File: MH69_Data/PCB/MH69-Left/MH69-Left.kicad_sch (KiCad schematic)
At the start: 85 parts, among them U1 nice_nano

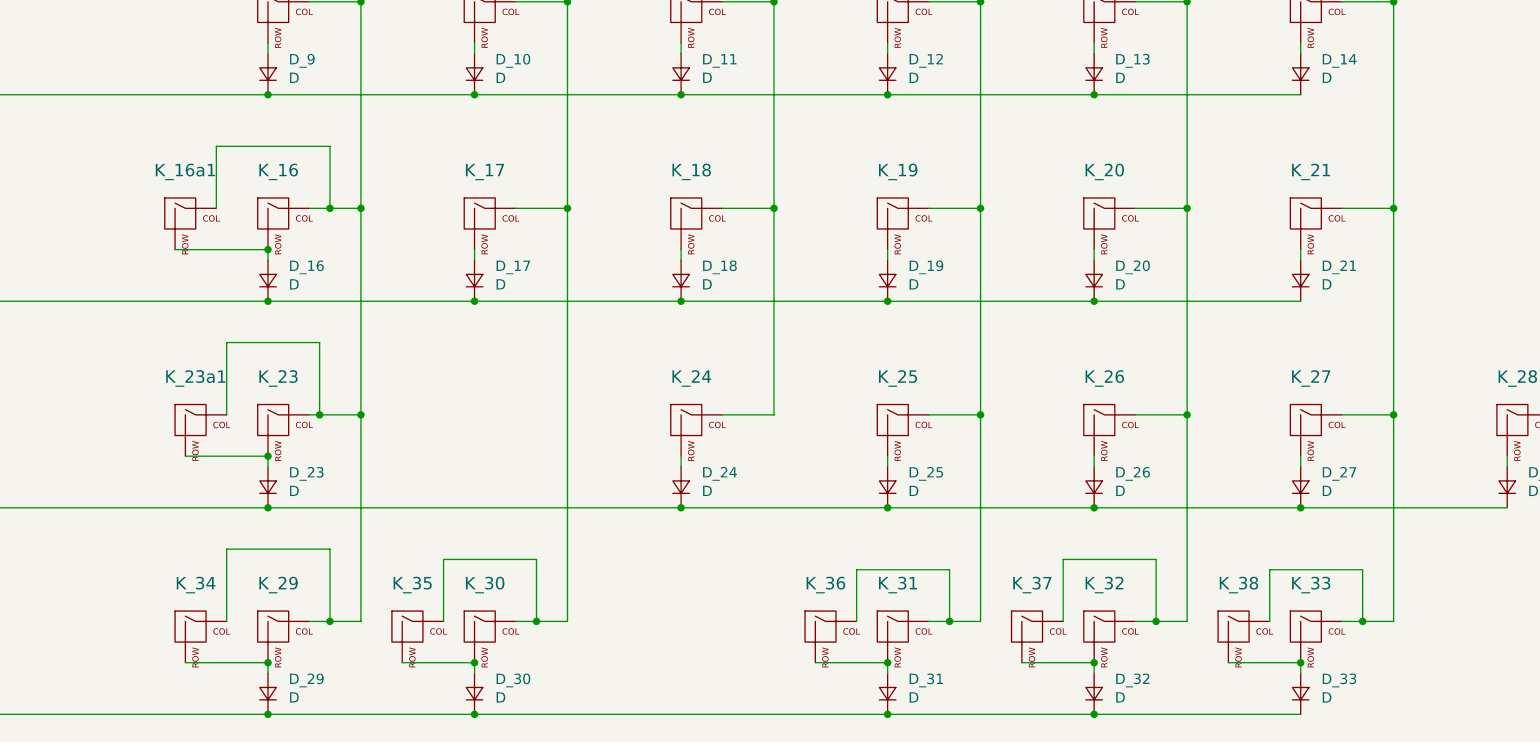
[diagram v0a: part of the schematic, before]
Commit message: Added Kailh Plated 1Us to Left
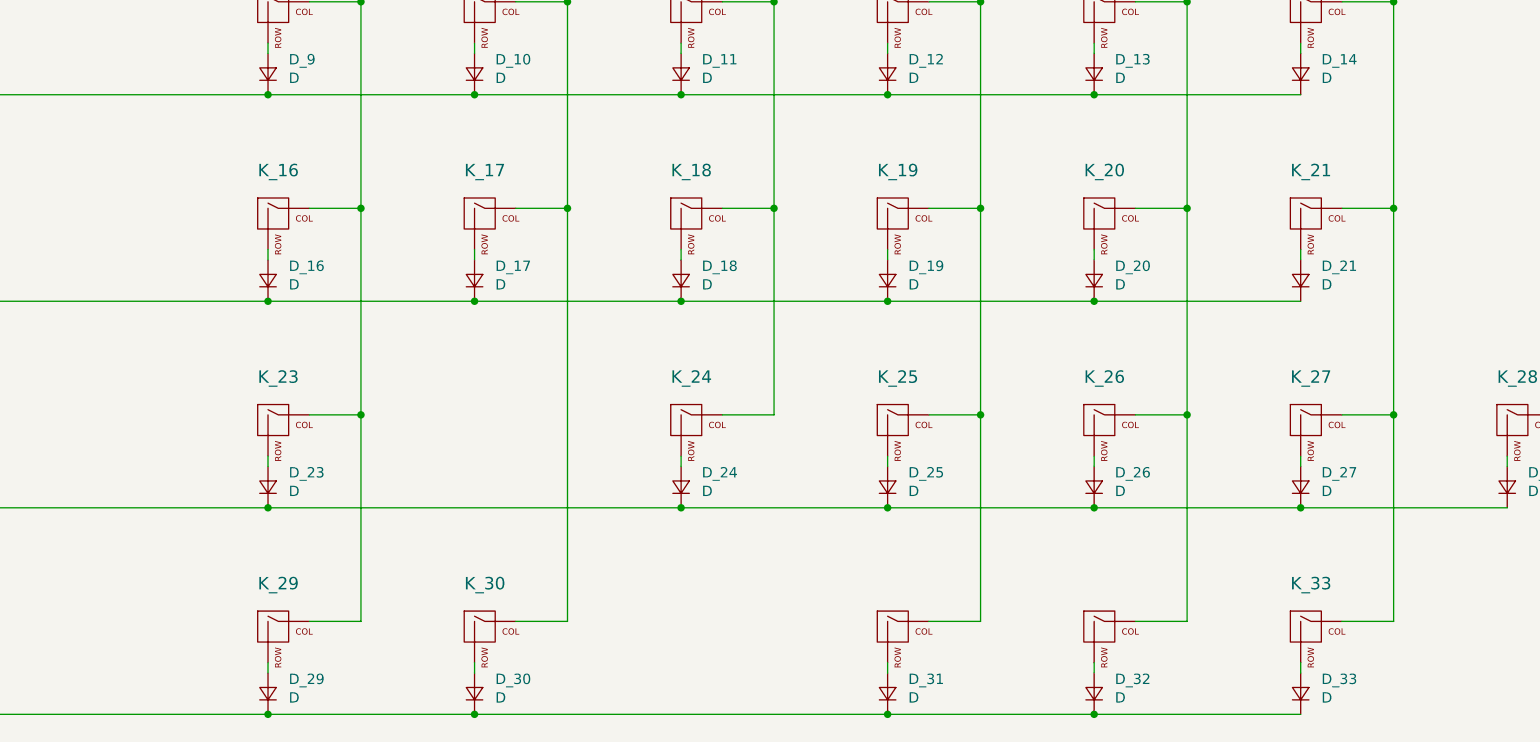
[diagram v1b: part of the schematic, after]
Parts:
- removed K_16a1: KEYSW, cb:Choc-MX-19mm-1.75u, symbol MX_Alps_Hybrid:MX-NoLED
- removed K_23a1: KEYSW, cb:Choc-MX-19mm-2.25u, symbol MX_Alps_Hybrid:MX-NoLED
- removed K_34, K_35, K_36, K_37, K_38: KEYSW, cb:Choc-MX-19mm-1.25u, symbol MX_Alps_Hybrid:MX-NoLED

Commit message: THE BIG CHANGE - schematic and PCB layout
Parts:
- added J1: OLED/E-Ink_L, Connector_PinHeader_2.54mm:PinHeader_1x05_P2.54mm_Vertical, symbol Connector_Generic:Conn_01x05
- Batt_L1: renamed from Batt1; footprint Connector_JST:JST_PH_B2B-PH-K_1x02_P2.00mm_Vertical -> Connector_PinHeader_2.54mm:PinHeader_1x02_P2.54mm_Vertical; symbol Connector:Conn_01x02_Socket -> Connector_Generic:Conn_01x02
- D_0, D_1, D_10, D_11, D_12, D_13, D_14, D_15, D_16, D_17, D_18, D_19, D_2, D_20, D_21, D_22, D_23, D_24, D_25, D_26, D_27, D_28, D_29, D_3, D_30, D_31, D_32, D_33, D_4, D_5, D_6, D_7, D_8, D_9: footprint ScottoKeebs_Components:Diode_DO-35 -> Diode_SMD:D_SOD-123
- H1, H2, H3, H4, H5, H6: footprint MountingHole:MountingHole_3.2mm_M3 -> ScottoKeebs_Scotto:Standoff_M2x6mm
- K_0, K_1, K_10, K_11, K_12, K_13, K_14, K_15, K_17, K_18, K_19, K_2, K_20, K_21, K_22, K_24, K_25, K_26, K_27, K_28, K_3, K_31, K_33, K_4, K_5, K_6, K_7, K_8: footprint cb:Choc-MX-19mm-1u -> PCM_Switch_Keyboard_Hotswap_Kailh:SW_Hotswap_Kailh_Choc_V1_Plated_1.00u
- K_16, K_23, K_30, K_32, K_9: footprint cb:Choc-MX-19mm-1.5u -> PCM_Switch_Keyboard_Hotswap_Kailh:SW_Hotswap_Kailh_Choc_V1_Plated_1.50u
- K_29: footprint cb:Choc-MX-19mm-1u -> PCM_Switch_Keyboard_Hotswap_Kailh:SW_Hotswap_Kailh_Choc_V1_Plated_1.25u
- PWR1: value POWER -> DIP_L; footprint Connector_JST:JST_PH_B2B-PH-K_1x02_P2.00mm_Vertical -> Button_Switch_SMD:SW_SPDT_PCM12; symbol Switch:SW_SPST -> Switch:SW_SPDT
- RST1: footprint Connector_JST:JST_PH_B2B-PH-K_1x02_P2.00mm_Vertical -> Button_Switch_SMD:SW_SPST_TL3342; symbol Switch:SW_SPST -> Switch:SW_Push
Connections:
- net CS_L: now reaches U1.1 (TX0/P0.06)
- net CS_L: now also J1.5 (Pin_5)
- net col2_L: now reaches U1.18 (AIN0/P0.02)
- net col2_L: now also K_10.1 (COL), K_17.1 (COL), K_2.1 (COL), K_30.1 (COL)
- net col1_L: now reaches U1.19 (AIN5/P0.29)
- net col1_L: now also K_1.1 (COL), K_16.1 (COL), K_23.1 (COL), K_29.1 (COL), K_9.1 (COL)
- net col0_L: now reaches U1.20 (AIN7/P0.31)
- net col0_L: now also K_0.1 (COL), K_15.1 (COL), K_22.1 (COL), K_8.1 (COL)
- net VCC: now reaches U1.21 (VCC)
- net VCC: now also J1.3 (Pin_3)
- net BOOT_L: now reaches RST1.1, U1.22 (RST)
- net GND: now reaches RST1.2, U1.23 (GND)
- net GND: now also Batt_L1.2 (Pin_2), U1.3 (GND), U1.4 (GND), J1.4 (Pin_4); no longer Batt_L1.1 (Pin_1)
- net at PWR1.2 (B): now also Batt_L1.1 (Pin_1); no longer U1.24 (BATIN/P0.04)
- net VBAT: now reaches PWR1.1 (A)
- net VBAT: now also U1.24 (BATIN/P0.04); no longer Batt_L1.2 (Pin_2)
- removed net col0: K_0.1 (COL), K_15.1 (COL), K_22.1 (COL), K_8.1 (COL), U1.5 (P0.17)
- removed net col1: K_1.1 (COL), K_16.1 (COL), K_23.1 (COL), K_29.1 (COL), K_9.1 (COL), U1.6 (P0.20)
- removed net col2: K_10.1 (COL), K_17.1 (COL), K_2.1 (COL), K_30.1 (COL), U1.7 (P0.22)
- net col3 renamed col3_L
- net col3_L: now also U1.17 (P1.15); no longer U1.8 (P0.24)
- net col4 renamed col4_L
- net col4_L: now also U1.16 (P1.13); no longer U1.9 (P1.00)
- net col5 renamed col5_L
- net col5_L: now also U1.15 (P1.11); no longer U1.10 (P0.11)
- net col6 renamed col6_L
- net col6_L: now also U1.14 (NFC2/P0.10); no longer U1.11 (P1.04)
- net col7 renamed col7_L
- net col7_L: now also U1.13 (NFC1/P0.09); no longer U1.12 (P1.06)
- net row0 renamed row0_L
- net row0_L: now also U1.11 (P1.04); no longer U1.17 (P1.15)
- net row1 renamed row1_L
- net row1_L: now also U1.10 (P0.11); no longer U1.16 (P1.13)
- net row2 renamed row2_L
- net row2_L: now also U1.9 (P1.00); no longer U1.13 (NFC1/P0.09)
- net row3 renamed row3_L
- net row3_L: now also U1.8 (P0.24); no longer U1.14 (NFC2/P0.10)
- net row4 renamed row4_L
- net row4_L: now also U1.7 (P0.22); no longer U1.15 (P1.11)
- new net SCL_L: J1.2 (Pin_2), U1.6 (P0.20)
- new net SDA_L: J1.1 (Pin_1), U1.5 (P0.17)
- no-connect marks 0 -> 6
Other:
- moved on the sheet: Batt_L1

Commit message: Left side finished?
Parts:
- added H7: MountingHole, ScottoKeebs_Scotto:Standoff_M2x6mm, symbol Mechanical:MountingHole
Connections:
- net col0_L: now also U1.14 (NFC2/P0.10); no longer U1.20 (AIN7/P0.31)
- net col1_L: now also U1.15 (P1.11); no longer U1.19 (AIN5/P0.29)
- net col2_L: now also U1.16 (P1.13); no longer U1.18 (AIN0/P0.02)
- net col4_L: now also U1.18 (AIN0/P0.02); no longer U1.16 (P1.13)
- net col5_L: now also U1.19 (AIN5/P0.29); no longer U1.15 (P1.11)
- net col6_L: now also U1.20 (AIN7/P0.31); no longer U1.14 (NFC2/P0.10)
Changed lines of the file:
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@@
 	(wire
 		(pts
-			(xy 298.45 73.66) (xy 303.53 73.66)
-		)
-		(stroke
-			(width 0)
-			(type default)
-		)
-	)
-	(wire
-		(pts
 			(xy 191.77 74.93) (xy 198.12 74.93)
 		)
@@
 	(wire
 		(pts
-			(xy 298.45 81.28) (xy 303.53 81.28)
-		)
-		(stroke
-			(width 0)
-			(type default)
-		)
-	)
-	(wire
-		(pts
 			(xy 298.45 60.96) (xy 303.53 60.96)
 		)
@@
 	(wire
 		(pts
-			(xy 298.45 78.74) (xy 303.53 78.74)
+			(xy 34.29 111.76) (xy 85.09 111.76)
 		)
 		(stroke
@@
 	(wire
 		(pts
-			(xy 298.45 71.12) (xy 303.53 71.12)
+			(xy 298.45 83.82) (xy 303.53 83.82)
 		)
 		(stroke
@@
 	(wire
 		(pts
-			(xy 34.29 111.76) (xy 85.09 111.76)
+			(xy 161.29 105.41) (xy 161.29 106.68)
 		)
 		(stroke
@@
 	(wire
 		(pts
-			(xy 161.29 105.41) (xy 161.29 106.68)
+			(xy 191.77 24.13) (xy 198.12 24.13)
 		)
 		(stroke
@@
 	(wire
 		(pts
-			(xy 191.77 24.13) (xy 198.12 24.13)
+			(xy 298.45 55.88) (xy 303.53 55.88)
 		)
 		(stroke
@@
 	(wire
 		(pts
-			(xy 298.45 55.88) (xy 303.53 55.88)
+			(xy 110.49 60.96) (xy 135.89 60.96)
 		)
 		(stroke
@@
 	(wire
 		(pts
-			(xy 110.49 60.96) (xy 135.89 60.96)
+			(xy 262.89 60.96) (xy 248.92 60.96)
 		)
 		(stroke
@@
 	(wire
 		(pts
-			(xy 262.89 60.96) (xy 248.92 60.96)
+			(xy 172.72 16.51) (xy 172.72 24.13)
 		)
 		(stroke
@@
 	(wire
 		(pts
-			(xy 172.72 16.51) (xy 172.72 24.13)
+			(xy 298.45 71.12) (xy 303.53 71.12)
 		)
 		(stroke
@@
 	(wire
 		(pts
-			(xy 298.45 68.58) (xy 303.53 68.58)
+			(xy 246.38 16.51) (xy 246.38 24.13)
 		)
 		(stroke
@@
 	(wire
 		(pts
-			(xy 246.38 16.51) (xy 246.38 24.13)
+			(xy 298.45 66.04) (xy 303.53 66.04)
 		)
 		(stroke
@@
 	(wire
 		(pts
-			(xy 298.45 76.2) (xy 303.53 76.2)
-		)
-		(stroke
-			(width 0)
-			(type default)
-		)
-	)
-	(wire
-		(pts
 			(xy 212.09 35.56) (xy 237.49 35.56)
 		)
@@
 	(wire
 		(pts
+			(xy 298.45 73.66) (xy 303.53 73.66)
+		)
+		(stroke
+			(width 0)
+			(type default)
+		)
+	)
+	(wire
+		(pts
 			(xy 115.57 49.53) (xy 121.92 49.53)
 		)
@@
 	(wire
 		(pts
+			(xy 298.45 68.58) (xy 303.53 68.58)
+		)
+		(stroke
+			(width 0)
+			(type default)
+		)
+	)
+	(wire
+		(pts
 			(xy 96.52 74.93) (xy 96.52 49.53)
 		)
@@
 	(wire
 		(pts
+			(xy 298.45 76.2) (xy 303.53 76.2)
+		)
+		(stroke
+			(width 0)
+			(type default)
+		)
+	)
+	(wire
+		(pts
 			(xy 161.29 130.81) (xy 161.29 132.08)
 		)
@@
 	(wire
 		(pts
-			(xy 298.45 83.82) (xy 303.53 83.82)
-		)
-		(stroke
-			(width 0)
-			(type default)
-		)
-	)
-	(wire
-		(pts
 			(xy 161.29 137.16) (xy 186.69 137.16)
 		)
@@
 	(wire
 		(pts
+			(xy 298.45 78.74) (xy 303.53 78.74)
+		)
+		(stroke
+			(width 0)
+			(type default)
+		)
+	)
+	(wire
+		(pts
 			(xy 260.35 81.28) (xy 262.89 81.28)
 		)
@@
 	(wire
 		(pts
-			(xy 110.49 29.21) (xy 110.49 30.48)
+			(xy 298.45 81.28) (xy 303.53 81.28)
 		)
 		(stroke
@@
 	(wire
 		(pts
-			(xy 298.45 66.04) (xy 303.53 66.04)
+			(xy 110.49 29.21) (xy 110.49 30.48)
 		)
 		(stroke
@@
 	(global_label "col2_L"
 		(shape input)
-		(at 303.53 71.12 0)
+		(at 303.53 76.2 0)
 		(effects
 			(font
@@
 		)
 		(property "Intersheetrefs" "${INTERSHEET_REFS}"
-			(at 303.53 71.12 0)
+			(at 303.53 76.2 0)
 			(effects
 				(font
@@
 	(global_label "col6_L"
 		(shape input)
-		(at 303.53 81.28 0)
+		(at 303.53 66.04 0)
 		(effects
 			(font
@@
 		)
 		(property "Intersheetrefs" "${INTERSHEET_REFS}"
-			(at 303.53 81.28 0)
+			(at 303.53 66.04 0)
 			(effects
 				(font
@@
 	(global_label "col1_L"
 		(shape input)
-		(at 303.53 68.58 0)
+		(at 303.53 78.74 0)
 		(effects
 			(font
@@
 		)
 		(property "Intersheetrefs" "${INTERSHEET_REFS}"
-			(at 303.53 68.58 0)
+			(at 303.53 78.74 0)
 			(effects
 				(font
@@
 	(global_label "col4_L"
 		(shape input)
-		(at 303.53 76.2 0)
+		(at 303.53 71.12 0)
 		(effects
 			(font
@@
 		)
 		(property "Intersheetrefs" "${INTERSHEET_REFS}"
-			(at 303.53 76.2 0)
+			(at 303.53 71.12 0)
 			(effects
 				(font
@@
 	(global_label "col5_L"
 		(shape input)
-		(at 303.53 78.74 0)
+		(at 303.53 68.58 0)
 		(effects
 			(font
@@
 		)
 		(property "Intersheetrefs" "${INTERSHEET_REFS}"
-			(at 303.53 78.74 0)
+			(at 303.53 68.58 0)
 			(effects
 				(font
@@
 	(global_label "col0_L"
 		(shape input)
-		(at 303.53 66.04 0)
+		(at 303.53 81.28 0)
 		(effects
 			(font
@@
 		)
 		(property "Intersheetrefs" "${INTERSHEET_REFS}"
-			(at 303.53 66.04 0)
+			(at 303.53 81.28 0)
 			(effects
 				(font
@@
 					(unit 1)
 				)
+			)
+		)
+	)
+	(symbol
+		(lib_id "Mechanical:MountingHole")
+		(at 354.33 43.18 0)
+		(unit 1)
+		(exclude_from_sim yes)
+		(in_bom no)
+		(on_board yes)
+		(dnp no)
+		(fields_autoplaced yes)
+		(property "Reference" "H7"
+			(at 356.87 41.9099 0)
+			(effects
+				(font
+					(size 1.27 1.27)
+				)
+				(justify left)
+			)
+		)
+		(property "Value" "MountingHole"
+			(at 356.87 44.4499 0)
+			(effects
+				(font
+					(size 1.27 1.27)
+				)
+				(justify left)
+			)
+		)
+		(property "Footprint" "ScottoKeebs_Scotto:Standoff_M2x6mm"
+			(at 354.33 43.18 0)
+			(effects
+				(font
+					(size 1.27 1.27)
+				)
+				(hide yes)
+			)
+		)
+		(property "Datasheet" "~"
+			(at 354.33 43.18 0)
+			(effects
+				(font
+					(size 1.27 1.27)
+				)
+				(hide yes)
+			)
+		)
+		(property "Description" "Mounting Hole without connection"
+			(at 354.33 43.18 0)
+			(effects
+				(font
+					(size 1.27 1.27)
+				)
+				(hide yes)
+			)
+		)
+		(instances
+			(project "MH69-Left"
+				(path "/ea7de392-007d-439a-bcfc-3322a1a7900b"
+					(reference "H7")
+					(unit 1)
+				)
